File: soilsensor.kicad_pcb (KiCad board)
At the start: 2 copper layers, 29 parts, among them J1 CONN_01X06, J2 BATT_CONN, P1 USB_OTG, U1 DS18B20, U2 RFD77101, U3 BQ24075, U4 MCP1700-3002E_SOT23, U5 TLC555

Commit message: working on pcb
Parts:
- J2: moved to B.Cu
- moved R6 16.3 mm to (104.4, 56.6), turned to 90 degrees
- moved R5 10.1 mm to (106.4, 56.6), turned to 90 degrees
- moved R4 7.97 mm to (107.2, 52.1), turned to 90 degrees
- moved J2 6.29 mm to (102.4, 58.2), turned to 90 degrees
- moved U4 5.85 mm to (104.1, 52.1)
- moved C4 3.34 mm to (115.6, 53.8)
- moved D1 2.65 mm to (96.3, 66.8)
- moved R8 2.54 mm to (97.8, 69.3)
- moved C3 2.50 mm to (100.1, 56.9), turned to 90 degrees
- moved R2 2.18 mm to (111.0, 61.0), turned to 0 degrees
- moved R9 2.09 mm to (106.2, 61.0)
- moved U3 1.78 mm to (109.7, 56.6), turned to 90 degrees
- moved C9 0.13 mm to (104.4, 114.6)
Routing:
- net +BATT: track 3.14 -> 11.7 mm
- net Net-(C9-Pad1): track 13.6 -> 20.0 mm
- net Net-(R6-Pad1): track 0.00 -> 5.54 mm
- net /PowerMgmt/~PGOOD: track 0.00 -> 5.37 mm
- net Net-(R5-Pad1): track 0.00 -> 2.08 mm
- net Net-(R8-Pad1): track 5.31 -> 3.47 mm
- net VDD: track 24.1 -> 25.8 mm
- net /CapacitiveSoilSensor/SensorOut: track 5.74 -> 4.28 mm
- net Net-(R7-Pad1): track 8.01 -> 7.35 mm

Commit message: finish pcb
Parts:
- moved U1 67.1 mm to (103.4, 144.3)
- moved J1 19.9 mm to (109.7, 35.1), turned to 180 degrees
- moved C1 16.0 mm to (112.5, 35.6), turned to 270 degrees
- moved U2 13.8 mm to (108.2, 41.9), turned to 270 degrees
- moved C5 11.7 mm to (109.7, 49.8), turned to 0 degrees
- moved C2 7.74 mm to (105.2, 50.5), turned to 180 degrees
- moved C9 6.10 mm to (104.6, 108.5)
- moved U4 5.64 mm to (109.7, 52.8), turned to 180 degrees
- moved P1 4.10 mm to (97.3, 49.0)
- moved C4 3.78 mm to (113.0, 51.1)
- moved R3 2.59 mm to (109.7, 47.5)
- moved R4 1.85 mm to (105.4, 52.6), turned to 180 degrees
- moved R9 0.51 mm to (106.2, 61.5)
- moved R7 0.25 mm to (104.1, 63.5)
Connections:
- U2 pad 24: /CapacitiveSoilSensor/SensorOut -> Net-(U2-Pad24)
- U2 pad 30: Net-(U2-Pad30) -> GND
- U2 pad 32: Net-(U2-Pad32) -> /CapacitiveSoilSensor/SensorOut
- U2 pad 39: Net-(U2-Pad39) -> VDD
- U2 pad 42: Net-(U2-Pad42) -> GND
- U2 pad 43: Net-(U2-Pad43) -> GND
- U2 pad 44: Net-(U2-Pad44) -> GND
- U2 pad 45: Net-(U2-Pad45) -> GND
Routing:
- net GND: track 67.0 -> 295.4 mm
- net Net-(R1-Pad1): track 26.5 -> 215.6 mm
- net VDD: track 25.8 -> 90.3 mm
- net /CapacitiveSoilSensor/SensorOut: track 4.28 -> 30.3 mm
- net /PowerMgmt/~CHG: track 0.00 -> 22.9 mm
- net /PowerMgmt/~PGOOD: track 5.37 -> 24.6 mm
- net Net-(C2-Pad1): track 0.00 -> 17.5 mm
- net Net-(C4-Pad1): track 0.00 -> 15.5 mm, vias 0 -> 2
- net /GPIO0: track 0.00 -> 15.4 mm
- net /GPIO1: track 0.00 -> 8.23 mm
- net /SWDCLK: track 0.00 -> 6.15 mm
- net Net-(C9-Pad1): track 20.0 -> 15.4 mm
- net /SWDIO/RESET: track 0.00 -> 4.42 mm
- net Net-(R4-Pad1): track 0.00 -> 3.80 mm
- net Net-(R7-Pad1): track 7.35 -> 8.81 mm
- added copper zone on F.Cu, net GND
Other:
- board outline added: 22.6 x 121.4 mm

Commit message: a lot of fixes, finished one-sided layout
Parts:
- removed R3: 100k, Resistors_SMD:R_0805_HandSoldering
- removed R4, R5: 1k, Resistors_SMD:R_0805_HandSoldering
- removed R6: 10k, Resistors_SMD:R_0805_HandSoldering
- R2: value 100k -> 10k
- U3: value BQ24075 -> MAX1811; footprint Housings_DFN_QFN:QFN-16-1EP_3x3mm_Pitch0.5mm -> Housings_SOIC:SOIC-8_3.9x4.9mm_Pitch1.27mm
- moved R2 13.1 mm to (108.0, 48.3), turned to 180 degrees
- moved C5 10.1 mm to (106.7, 59.4)
- moved U4 5.39 mm to (105.9, 56.6), turned to 270 degrees
- moved U3 4.60 mm to (109.2, 52.1), turned to 0 degrees
- moved C2 4.19 mm to (101.1, 49.5), turned to 270 degrees
- moved C4 2.50 mm to (114.0, 53.3)
- moved R7 2.05 mm to (106.2, 63.8)
- moved U5 0.77 mm to (104.9, 67.6)
- moved R9 0.25 mm to (106.2, 61.7)
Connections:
- C4 pad 1: Net-(C4-Pad1) -> +BATT
- P1 pad 2: Net-(P1-Pad2) -> (no net)
- P1 pad 3: Net-(P1-Pad3) -> (no net)
- P1 pad 4: Net-(P1-Pad4) -> (no net)
- R2 pad 1: VDD -> /PowerMgmt/EN
- R2 pad 2: /PowerMgmt/~PGOOD -> Net-(C2-Pad1)
- U2 pad 10: Net-(U2-Pad10) -> (no net)
- U2 pad 11: Net-(U2-Pad11) -> (no net)
- U2 pad 12: Net-(U2-Pad12) -> (no net)
- U2 pad 13: Net-(U2-Pad13) -> (no net)
- U2 pad 14: Net-(U2-Pad14) -> (no net)
- U2 pad 15: Net-(U2-Pad15) -> (no net)
- U2 pad 16: Net-(U2-Pad16) -> (no net)
- U2 pad 17: Net-(U2-Pad17) -> (no net)
- U2 pad 18: Net-(U2-Pad18) -> (no net)
- U2 pad 20: Net-(U2-Pad20) -> (no net)
- U2 pad 21: Net-(U2-Pad21) -> (no net)
- U2 pad 22: Net-(U2-Pad22) -> (no net)
- U2 pad 24: Net-(U2-Pad24) -> (no net)
- U2 pad 27: Net-(U2-Pad27) -> (no net)
- U2 pad 28: Net-(U2-Pad28) -> (no net)
- U2 pad 29: Net-(U2-Pad29) -> (no net)
- U2 pad 3: Net-(U2-Pad3) -> (no net)
- U2 pad 31: Net-(U2-Pad31) -> (no net)
- U2 pad 33: Net-(U2-Pad33) -> (no net)
- U2 pad 34: Net-(U2-Pad34) -> (no net)
- U2 pad 35: Net-(U2-Pad35) -> (no net)
- U2 pad 36: Net-(U2-Pad36) -> (no net)
- U2 pad 37: Net-(U2-Pad37) -> (no net)
- U2 pad 38: Net-(U2-Pad38) -> GND
- U2 pad 39: VDD -> /PowerMgmt/EN
- U2 pad 41: /PowerMgmt/~PGOOD -> VDD
- U2 pad 5: Net-(U2-Pad5) -> (no net)
- U3 pad 1: Net-(R6-Pad1) -> Net-(C2-Pad1)
- U3 pad 2: +BATT -> GND
- U3 pad 3: +BATT -> GND
- U3 pad 4: GND -> Net-(C2-Pad1)
- U3 pad 5: Net-(C4-Pad1) -> +BATT
- U3 pad 7: /PowerMgmt/~PGOOD -> /PowerMgmt/EN
- U3 pad 8: GND -> /PowerMgmt/~CHG
- U4 pad 3: Net-(C4-Pad1) -> +BATT
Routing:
- net /PowerMgmt/~PGOOD: track 24.6 -> 0.00 mm
- net VDD: track 90.3 -> 67.1 mm
- net GND: track 295.4 -> 316.8 mm
- net /PowerMgmt/~CHG: track 22.9 -> 6.57 mm
- net Net-(C4-Pad1): track 15.5 -> 0.00 mm, vias 2 -> 0
- net /PowerMgmt/EN: track 0.00 -> 8.09 mm
- net +BATT: track 11.7 -> 18.4 mm
- net Net-(R6-Pad1): track 5.54 -> 0.00 mm
- net Net-(R4-Pad1): track 3.80 -> 0.00 mm
- net Net-(R5-Pad1): track 2.08 -> 0.00 mm
- net Net-(C8-Pad1): track 13.1 -> 11.6 mm
- net Net-(R7-Pad1): track 8.81 -> 9.89 mm
- net Net-(C2-Pad1): track 17.5 -> 16.5 mm
- net Net-(C6-Pad1): track 2.91 -> 2.20 mm

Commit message: update sensor
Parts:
- removed R10: 1M, Resistors_SMD:R_0805_HandSoldering
- removed R7: 1.6k, Resistors_SMD:R_0805_HandSoldering
- removed R8: 10k, Resistors_SMD:R_0805_HandSoldering
- removed R9: 330, Resistors_SMD:R_0805_HandSoldering
- added R3: 1.6k, Resistors_SMD:R_0603_HandSoldering, F.Cu at (106.9, 63.8)
- added R4: 10k, Resistors_SMD:R_0603_HandSoldering, F.Cu at (99.1, 68.3)
- added R5: 330, Resistors_SMD:R_0603_HandSoldering, F.Cu at (106.9, 62.0)
- added R6: 1M, Resistors_SMD:R_0603_HandSoldering, F.Cu at (99.1, 65.5)
- C1, C10: footprint Capacitors_SMD:C_0805_HandSoldering -> Capacitors_SMD:C_1206_HandSoldering
- C6, C7, C8: footprint Capacitors_SMD:C_0805_HandSoldering -> Capacitors_SMD:C_0603_HandSoldering
- R1, R2: footprint Resistors_SMD:R_0805_HandSoldering -> Resistors_SMD:R_0603_HandSoldering
- moved C10 2.75 mm to (100.1, 63.2)
- moved C1 2.34 mm to (114.8, 36.1)
- moved J1 1.37 mm to (111.0, 35.6)
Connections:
- J1 pad 4: /GPIO0 -> /GPIO1
- J1 pad 5: /GPIO1 -> /GPIO0
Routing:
- net GND: track 316.8 -> 292.9 mm
- net /GPIO0: track 15.4 -> 8.36 mm
- net VDD: track 67.1 -> 71.4 mm
- net Net-(R3-Pad1): track 9.89 -> 7.62 mm
- net Net-(C9-Pad1): track 15.4 -> 17.3 mm
- net /SWDCLK: track 6.15 -> 4.67 mm
- net /CapacitiveSoilSensor/SensorOut: track 29.8 -> 31.2 mm
- net Net-(R4-Pad1): track 3.54 -> 2.09 mm
- net /GPIO1: track 8.23 -> 7.20 mm
- net /SWDIO/RESET: track 4.42 -> 3.38 mm
- net Net-(C8-Pad1): track 11.6 -> 12.2 mm

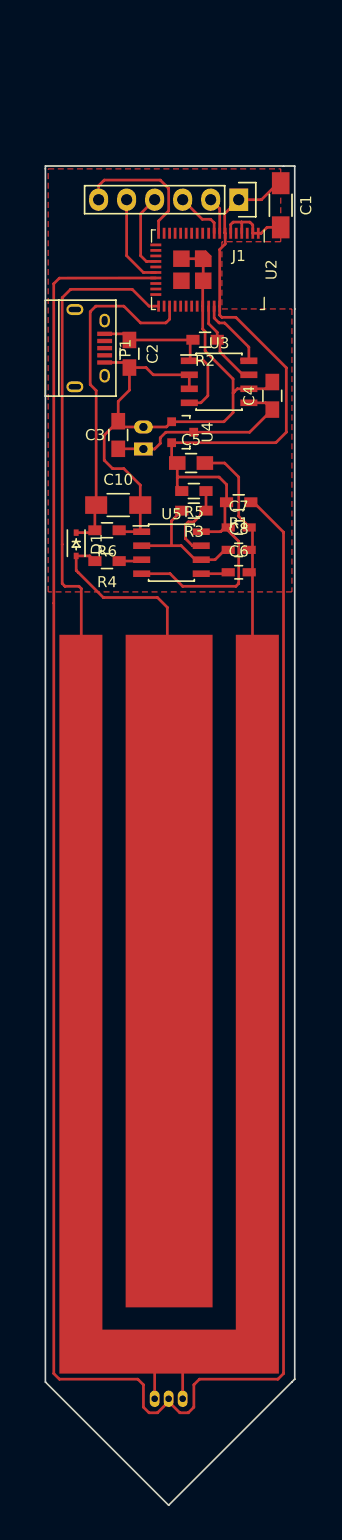
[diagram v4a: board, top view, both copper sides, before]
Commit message: update pcb for new schematic
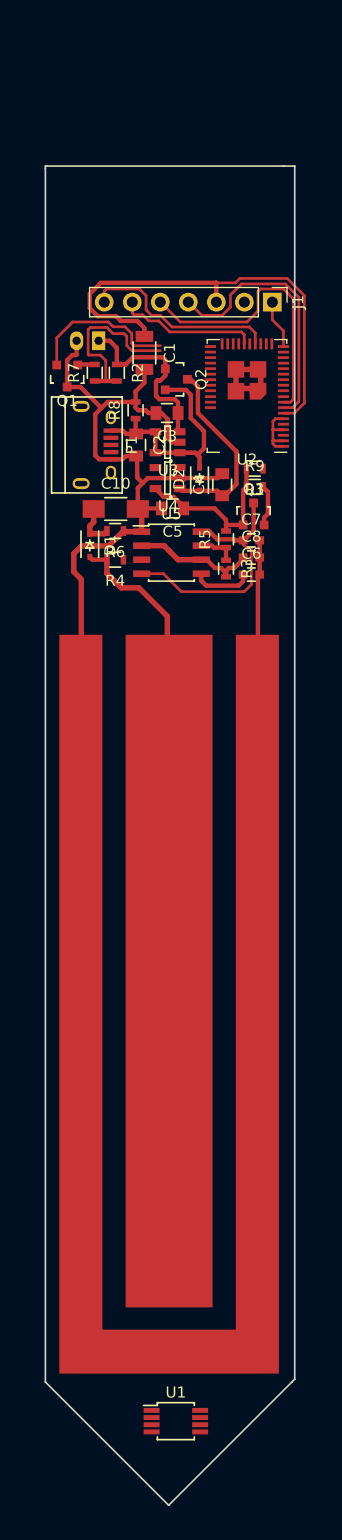
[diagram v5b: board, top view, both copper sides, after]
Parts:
- added D2: BAT20J, Diodes_SMD:SOD-323, F.Cu at (107.5, 60.9)
- added Q1: Q_NMOS_DGS, TO_SOT_Packages_SMD:SOT-23, F.Cu at (95.5, 51.5)
- added Q2: Q_PMOS_DGS, TO_SOT_Packages_SMD:SOT-23, F.Cu at (105.3, 51.9)
- added Q3: Q_PMOS_DGS, TO_SOT_Packages_SMD:SOT-23, F.Cu at (112.3, 64.0)
- added R7: 8.2k, Resistors_SMD:R_0603, F.Cu at (98.0, 51.2)
- added R8: 10k, Resistors_SMD:R_0603, F.Cu at (101.7, 54.6)
- added R9: 10k, Resistors_SMD:R_0603, F.Cu at (112.5, 61.6)
- C1: footprint Capacitors_SMD:C_1206_HandSoldering -> Capacitors_SMD:C_1206
- C2, C4: footprint Capacitors_SMD:C_0805_HandSoldering -> Capacitors_SMD:C_0805
- C3: value 22u -> 4.7u; footprint Capacitors_SMD:C_0805_HandSoldering -> Capacitors_SMD:C_0805
- C5: value 1u -> 2.2u; footprint Capacitors_SMD:C_0805_HandSoldering -> Capacitors_SMD:C_0805
- C6, C7, C8: footprint Capacitors_SMD:C_0603_HandSoldering -> Capacitors_SMD:C_0603
- J1: value CONN_01X06 -> CONN_01X07; footprint Socket_Strips:Socket_Strip_Straight_1x06 -> Pin_Headers:Pin_Header_Straight_1x07_Pitch2.54mm
- R1, R3, R4, R5, R6: footprint Resistors_SMD:R_0603_HandSoldering -> Resistors_SMD:R_0603
- R2: value 10k -> 3.3k; footprint Resistors_SMD:R_0603_HandSoldering -> Resistors_SMD:R_0603
- U1: footprint TO_SOT_Packages_THT:TO-92_Inline_Narrow_Oval -> Housings_SSOP:MSOP-8_3x3mm_Pitch0.65mm; moved to F.Cu
- U3: value MAX1811 -> MCP73811T; footprint Housings_SOIC:SOIC-8_3.9x4.9mm_Pitch1.27mm -> TO_SOT_Packages_SMD:SOT-23-5
- U4: value MCP1700-3002E_SOT23 -> AP2204K-3.0; footprint TO_SOT_Packages_SMD:SOT-23 -> TO_SOT_Packages_SMD:SOT-23-5
- moved C1 18.2 mm to (102.5, 49.5)
- moved U2 12.0 mm to (111.8, 53.4), turned to 180 degrees
- moved J2 10.6 mm to (98.3, 48.4), turned to 180 degrees
- moved J1 9.78 mm to (114.0, 44.9), turned to 270 degrees
- moved C4 9.25 mm to (109.5, 61.4)
- moved P1 8.80 mm to (97.8, 57.8)
- moved R2 8.54 mm to (100.0, 51.2), turned to 270 degrees
- moved C2 8.29 mm to (101.7, 57.8)
- moved U3 7.20 mm to (104.5, 57.5), turned to 180 degrees
- moved R3 6.00 mm to (109.8, 69.0), turned to 270 degrees
- moved R5 5.26 mm to (109.8, 66.3), turned to 90 degrees
- moved C3 4.85 mm to (104.5, 54.9), turned to 180 degrees
- moved C5 4.44 mm to (105.0, 63.5), turned to 180 degrees
- moved U4 4.38 mm to (104.5, 60.8), turned to 180 degrees
- moved R1 3.37 mm to (112.5, 60.0)
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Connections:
- C4 pad 1: +BATT -> Net-(C4-Pad1)
- C7 pad 1: VDD -> Net-(C7-Pad1)
- J1 pad 1: VDD -> GND
- J1 pad 2: /SWDIO/RESET -> (no net)
- J1 pad 3: /SWDCLK -> VDD
- J1 pad 4: /GPIO1 -> /SWDIO/RESET
- J1 pad 5: /GPIO0 -> /SWDCLK
- J1 pad 6: GND -> /GPIO0
- R2 pad 1: /PowerMgmt/EN -> +BATT
- R2 pad 2: Net-(C2-Pad1) -> /PowerMgmt/BATT_V
- U2 pad 20: (no net) -> /CapacitiveSoilSensor/~EN
- U2 pad 24: (no net) -> /PowerMgmt/BATT_V
- U2 pad 39: /PowerMgmt/EN -> (no net)
- U2 pad 40: /PowerMgmt/~CHG -> /PowerMgmt/BATT_V_EN
- U3 pad 3: GND -> +BATT
- U3 pad 5: +BATT -> Net-(C2-Pad1)
- U4 pad 1: GND -> Net-(C4-Pad1)
- U4 pad 2: VDD -> GND
- U4 pad 3: +BATT -> (no net)
- U5 pad 4: VDD -> Net-(C7-Pad1)
- U5 pad 8: VDD -> Net-(C7-Pad1)
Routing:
- net Net-(R1-Pad1): track 215.6 -> 0.00 mm
- net GND: track 292.9 -> 95.4 mm
- net /CapacitiveSoilSensor/SensorOut: track 31.2 -> 4.70 mm
- net Net-(C7-Pad1): track 0.00 -> 23.4 mm
- net /SWDCLK: track 4.67 -> 25.6 mm
- net /SWDIO/RESET: track 3.38 -> 23.9 mm
- net Net-(C4-Pad1): track 0.00 -> 17.4 mm
- net /PowerMgmt/BATT_V: track 0.00 -> 15.9 mm
- net /PowerMgmt/BATT_V_EN: track 0.00 -> 13.9 mm
- net VDD: track 71.4 -> 57.7 mm
- net /GPIO1: track 7.20 -> 18.2 mm
- net /PowerMgmt/EN: track 8.02 -> 0.00 mm
- net /PowerMgmt/~CHG: track 6.57 -> 0.00 mm
- net Net-(C2-Pad1): track 16.5 -> 21.4 mm
- net /GPIO0: track 8.36 -> 12.8 mm
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- removed copper zone on F.Cu, net GND

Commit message: create new one-sided pcb
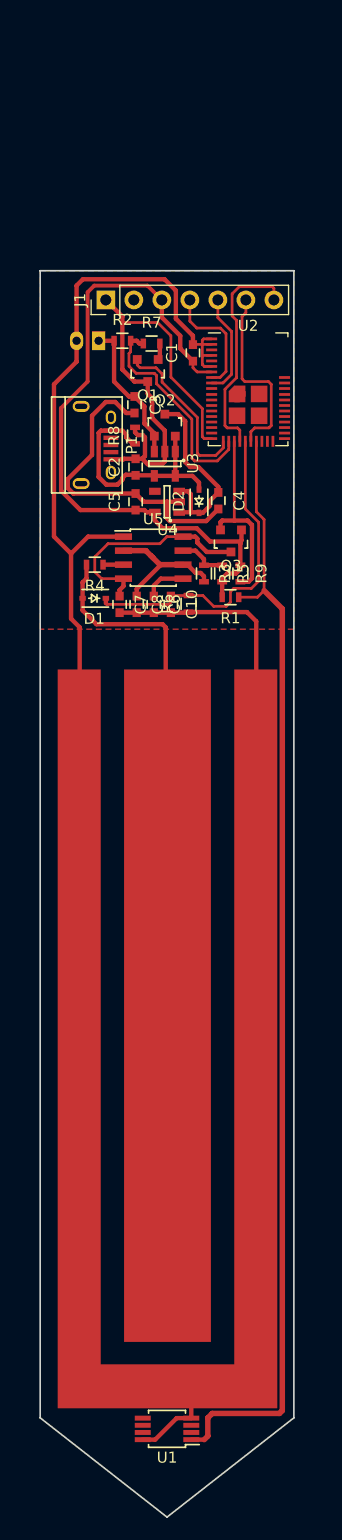
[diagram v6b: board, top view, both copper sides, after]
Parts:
- C1: footprint Capacitors_SMD:C_1206 -> Capacitors_SMD:C_0603
- C10: footprint Capacitors_SMD:C_1206_HandSoldering -> Capacitors_SMD:C_0603
- C2, C3, C4, C5: footprint Capacitors_SMD:C_0805 -> Capacitors_SMD:C_0603
- U1: value DS18B20 -> DS18B20U
- moved J1 15.1 mm to (99.0, 44.6), turned to 90 degrees
- moved C7 13.3 mm to (100.2, 72.2), turned to 270 degrees
- moved R1 11.9 mm to (110.2, 71.6)
- moved C8 11.2 mm to (101.8, 72.2), turned to 270 degrees
- moved C10 9.99 mm to (104.8, 72.2), turned to 270 degrees
- moved R6 9.37 mm to (106.5, 72.2), turned to 90 degrees
- moved C6 9.25 mm to (103.3, 72.2), turned to 270 degrees
- moved R9 7.96 mm to (111.2, 69.5), turned to 270 degrees
- moved Q1 7.32 mm to (102.8, 51.0)
- moved R7 5.79 mm to (103.1, 48.6), turned to 0 degrees
- moved D1 4.82 mm to (97.9, 71.7), turned to 180 degrees
- moved C1 4.40 mm to (106.8, 49.5), turned to 90 degrees
- moved Q2 4.28 mm to (104.3, 56.0), turned to 0 degrees
- moved C5 3.40 mm to (101.7, 63.0), turned to 90 degrees
- moved Q3 3.19 mm to (110.3, 66.5), turned to 180 degrees
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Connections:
- U1 pad 1: GND -> Net-(R1-Pad1)
- U1 pad 2: Net-(R1-Pad1) -> (no net)
- U1 pad 3: GND -> (no net)
- U1 pad 4: (no net) -> GND
- U1 pad 8: (no net) -> GND
- U2 pad 20: /CapacitiveSoilSensor/~EN -> /PowerMgmt/BATT_V_EN
- U2 pad 21: (no net) -> /PowerMgmt/BATT_V
- U2 pad 22: (no net) -> /CapacitiveSoilSensor/~EN
- U2 pad 24: /PowerMgmt/BATT_V -> /CapacitiveSoilSensor/SensorOut
- U2 pad 32: /CapacitiveSoilSensor/SensorOut -> (no net)
- U2 pad 38: GND -> (no net)
- U2 pad 40: /PowerMgmt/BATT_V_EN -> (no net)
- U2 pad 41: VDD -> (no net)
- U4 pad 3: (no net) -> Net-(C4-Pad1)
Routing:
- net GND: track 95.4 -> 233.9 mm
- net Net-(R1-Pad1): track 0.00 -> 101.7 mm
- net /CapacitiveSoilSensor/SensorOut: track 4.70 -> 30.1 mm
- net /SWDCLK: track 25.6 -> 9.39 mm
- net /SWDIO/RESET: track 23.9 -> 10.6 mm
- net /CapacitiveSoilSensor/~EN: track 3.78 -> 17.0 mm
- net Net-(C9-Pad1): track 13.6 -> 18.2 mm
- net /GPIO0: track 12.8 -> 16.8 mm
- net /PowerMgmt/BATT_V: track 15.9 -> 19.9 mm
- net VDD: track 57.7 -> 61.6 mm
- net +BATT: track 17.0 -> 13.3 mm
- net Net-(C7-Pad1): track 23.4 -> 19.8 mm
- net /GPIO1: track 18.2 -> 20.3 mm
- net Net-(R4-Pad1): track 0.18 -> 2.03 mm
- net Net-(C6-Pad1): track 5.38 -> 3.86 mm
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- added copper zone on F.Cu, net GND
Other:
- board size 22.6 x 121.4 mm -> 23 x 113 mm

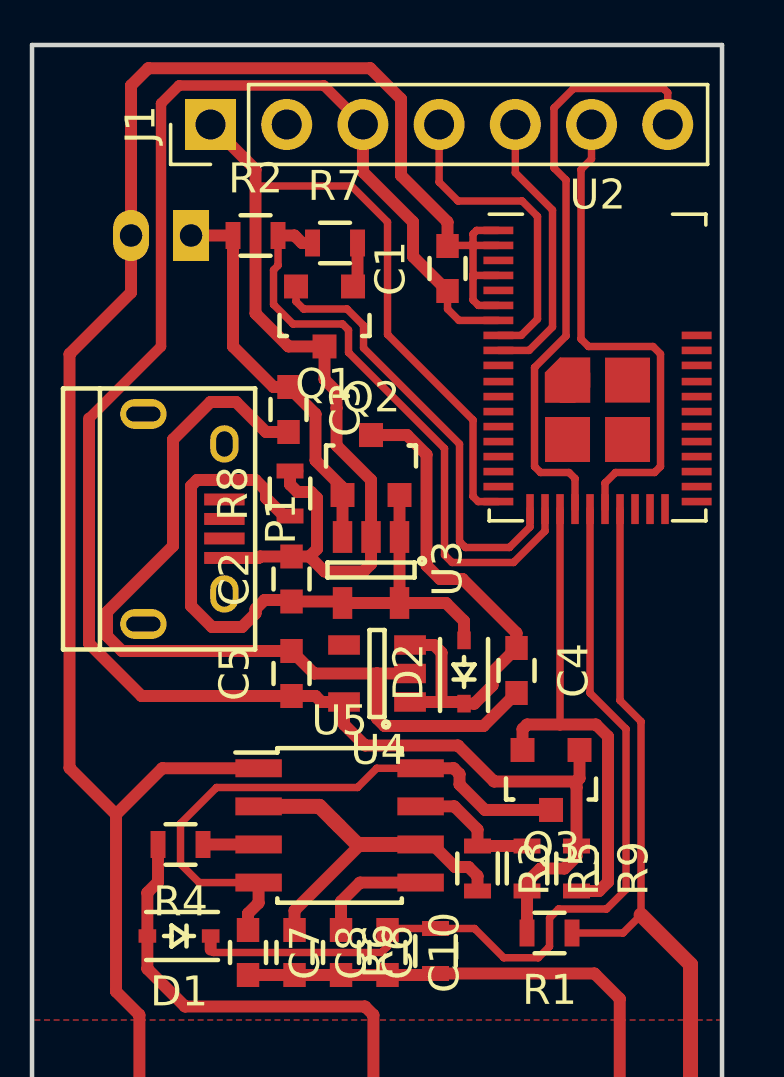
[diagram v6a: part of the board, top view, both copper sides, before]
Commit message: update pcb with new mosfets
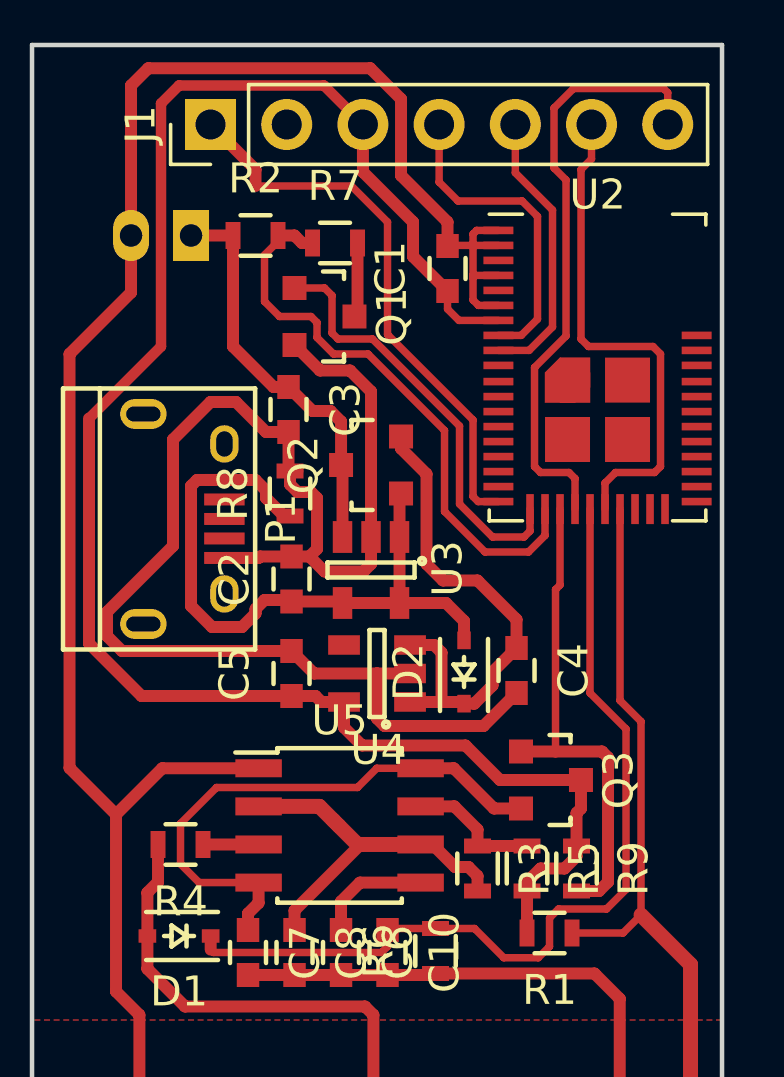
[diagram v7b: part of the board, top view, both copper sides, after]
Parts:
- Q1: value Q_NMOS_DGS -> Q_NMOS_GSD
- Q2, Q3: value Q_PMOS_DGS -> Q_PMOS_GSD
- turned Q1 to 270 degrees
- turned Q2 to 90 degrees
- turned Q3 to 270 degrees
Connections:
- Q1 pad 1: Net-(Q1-Pad1) -> /PowerMgmt/BATT_V_EN
- Q1 pad 2: /PowerMgmt/BATT_V_EN -> GND
- Q1 pad 3: GND -> Net-(Q1-Pad3)
- Q2 pad 1: +BATT -> Net-(C2-Pad1)
- Q2 pad 2: Net-(C2-Pad1) -> Net-(C4-Pad1)
- Q2 pad 3: Net-(C4-Pad1) -> +BATT
- Q3 pad 1: VDD -> /CapacitiveSoilSensor/~EN
- Q3 pad 2: /CapacitiveSoilSensor/~EN -> Net-(C7-Pad1)
- Q3 pad 3: Net-(C7-Pad1) -> VDD
- R7 pad 2: Net-(Q1-Pad1) -> Net-(Q1-Pad3)
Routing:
- net GND: track 233.9 -> 229.2 mm
- net Net-(Q1-Pad3): track 0.00 -> 2.49 mm
- net Net-(Q1-Pad1): track 1.51 -> 0.00 mm
- net Net-(C7-Pad1): track 19.8 -> 18.6 mm
- net Net-(C4-Pad1): track 17.7 -> 16.7 mm
- net VDD: track 61.6 -> 60.8 mm
- net /PowerMgmt/BATT_V_EN: track 14.9 -> 14.4 mm
- net /CapacitiveSoilSensor/~EN: track 17.0 -> 16.4 mm

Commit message: update pcb
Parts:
- P1: footprint Connect:USB_Micro-B -> Connectors_USB:USB_Micro-B_Molex_47346-0001
- moved C2 8.00 mm to (99.2, 52.2)
- moved P1 5.12 mm to (94.5, 54.0)
- moved R8 3.16 mm to (99.2, 55.0), turned to 270 degrees
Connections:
- C4 pad 1: Net-(C4-Pad1) -> VBUS
- D2 pad 1: Net-(C4-Pad1) -> VBUS
- J1 pad 3: VDD -> VBUS
- Q2 pad 2: Net-(C4-Pad1) -> VBUS
- U4 pad 1: Net-(C4-Pad1) -> VBUS
- U4 pad 3: Net-(C4-Pad1) -> VBUS
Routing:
- net GND: track 229.2 -> 162.1 mm
- net VDD: track 60.8 -> 20.1 mm
- net VBUS: track 0.00 -> 16.7 mm
- net Net-(C4-Pad1): track 16.7 -> 0.00 mm
- net Net-(C2-Pad1): track 22.5 -> 10.3 mm
- net +BATT: track 13.6 -> 7.50 mm
